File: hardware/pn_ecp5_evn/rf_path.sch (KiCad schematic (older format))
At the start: 46 parts, among them J701 Conn_Coaxial, J702 Conn_Coaxial, J703 Conn_Coaxial, U701 SYM-63LH+, U702 ADG621, U703 OPA2211

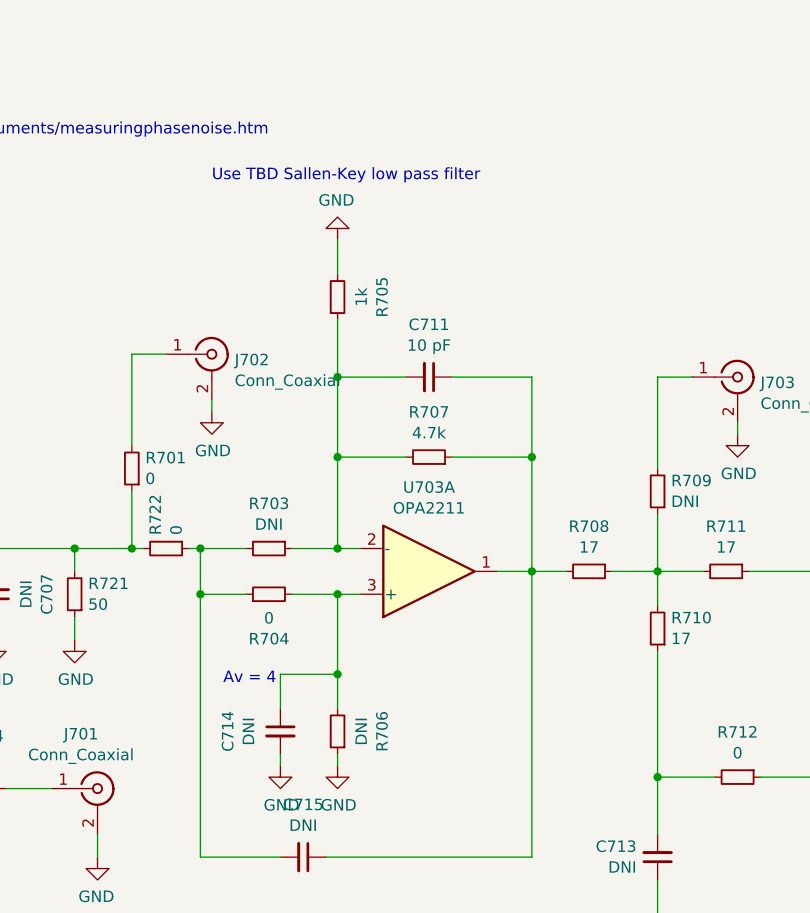
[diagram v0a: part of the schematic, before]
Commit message: fixed rectifier circuit, inverted first lna to cancel out inverting integrator..
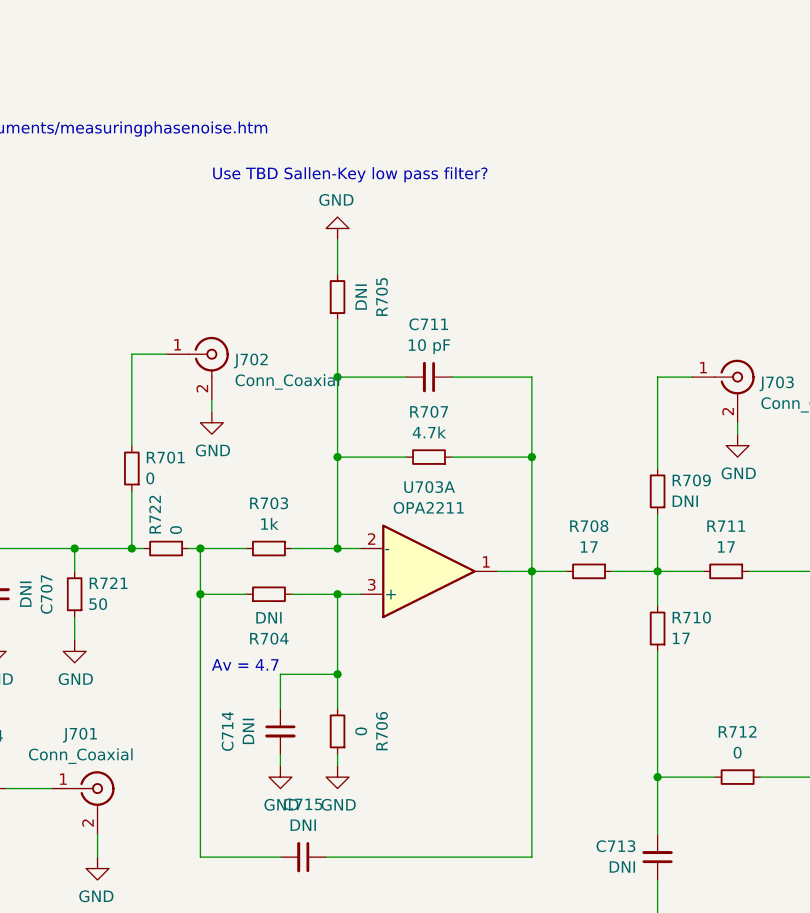
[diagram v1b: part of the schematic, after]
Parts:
- R703: value DNI -> 1k
- R704: value 0 -> DNI
- R705: value 1k -> DNI
- R706: value DNI -> 0
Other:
- note added: "Av = 4.7"
- note added: "Use TBD Sallen-Key low pass filter?\n"
- note removed: "Av = 4"
- note removed: "Use TBD Sallen-Key low pass filter"
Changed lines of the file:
@@
 Wire Wire Line
 	5600 2800 5600 3300
-Text Notes 4250 3800 0    50   ~ 0
-Av = 4
+Text Notes 4200 3750 0    50   ~ 0
+Av = 4.7
 Text Notes 5900 5900 0    50   ~ 0
 want to be able to measure -160 dBc/Hz signal @ 1 MHz offset\nassume max convserion loss of 10 dB, 0 dBm input\n-170 dBc/Hz..\n\nADC has 100 dB SFDR, 2.5 MSPS (60 dB gain), so DANL of 160 dBFS/Hz\nfull scale is 5Vpp 100 ohms, so 15 dBm\nDANL of 145 dBm/Hz\nNeed about 25 dB of gain
@@
 P 4450 3200
 F 0 "R703" V 4254 3200 50  0000 C CNN
-F 1 "DNI" V 4345 3200 50  0000 C CNN
+F 1 "1k" V 4345 3200 50  0000 C CNN
 F 2 "Resistor_SMD:R_0402_1005Metric" H 4450 3200 50  0001 C CNN
 F 3 "~" H 4450 3200 50  0001 C CNN
@@
 P 4750 2100
 F 0 "R705" V 4946 2100 50  0000 C CNN
-F 1 "1k" V 4855 2100 50  0000 C CNN
+F 1 "DNI" V 4855 2100 50  0000 C CNN
 F 2 "Resistor_SMD:R_0402_1005Metric" H 4750 2100 50  0001 C CNN
 F 3 "~" H 4750 2100 50  0001 C CNN
@@
 P 4750 4000
 F 0 "R706" V 4554 4000 50  0000 C CNN
-F 1 "DNI" V 4645 4000 50  0000 C CNN
+F 1 "0" V 4645 4000 50  0000 C CNN
 F 2 "Resistor_SMD:R_0402_1005Metric" H 4750 4000 50  0001 C CNN
 F 3 "~" H 4750 4000 50  0001 C CNN
@@
 P 4450 3400
 F 0 "R704" V 4254 3400 50  0000 C CNN
-F 1 "0" V 4345 3400 50  0000 C CNN
+F 1 "DNI" V 4345 3400 50  0000 C CNN
 F 2 "Resistor_SMD:R_0402_1005Metric" H 4450 3400 50  0001 C CNN
 F 3 "~" H 4450 3400 50  0001 C CNN
@@
 	3250 3300 3250 3200
 Text Notes 4200 1600 0    50   ~ 0
-Use TBD Sallen-Key low pass filter
+Use TBD Sallen-Key low pass filter?\n
 $Comp
 L Device:C_Small C715
